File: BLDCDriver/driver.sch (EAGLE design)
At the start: 7 parts, among them U1 QFN50P400X400X100-25NDRV8300D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

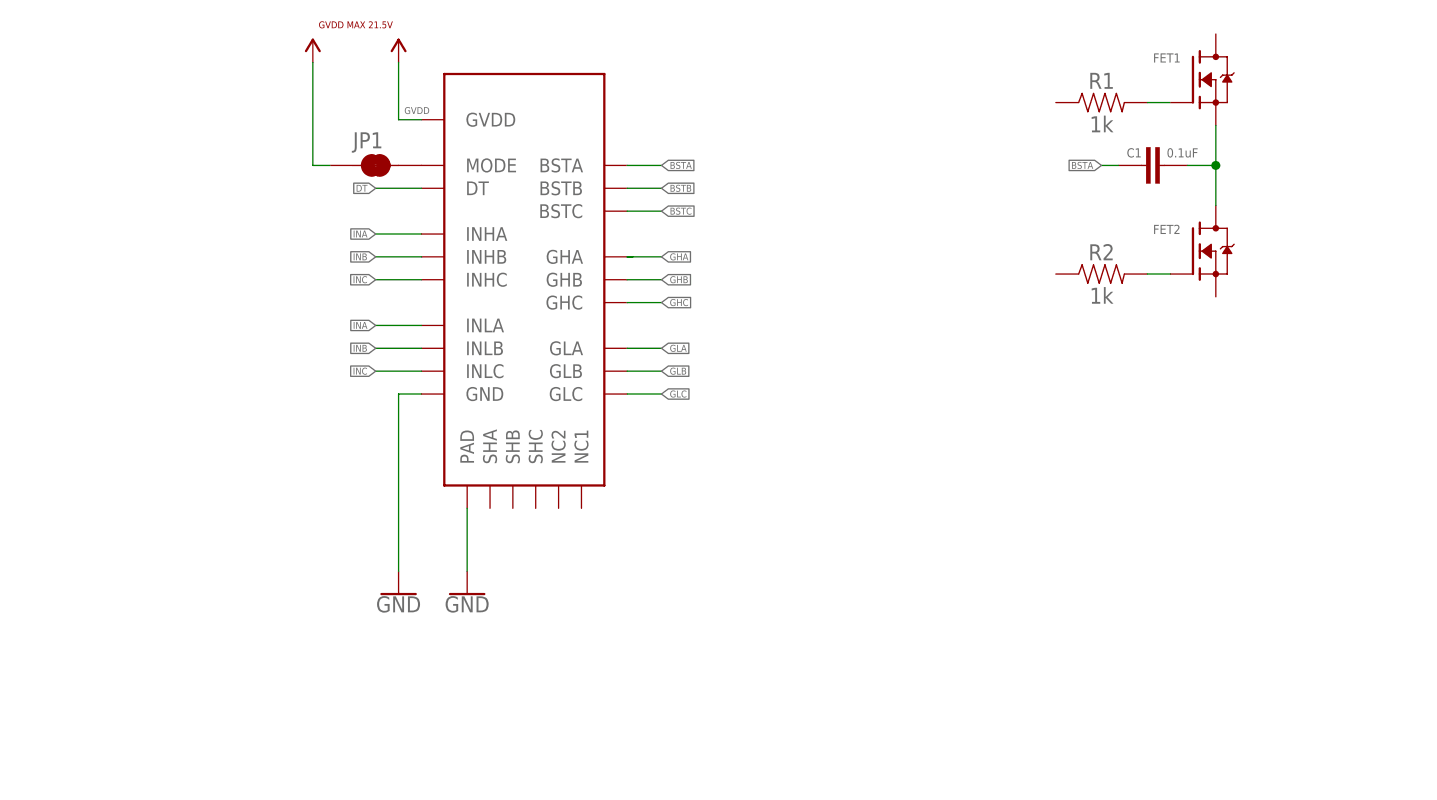
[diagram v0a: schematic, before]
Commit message: add MOSFETs on driver schematic
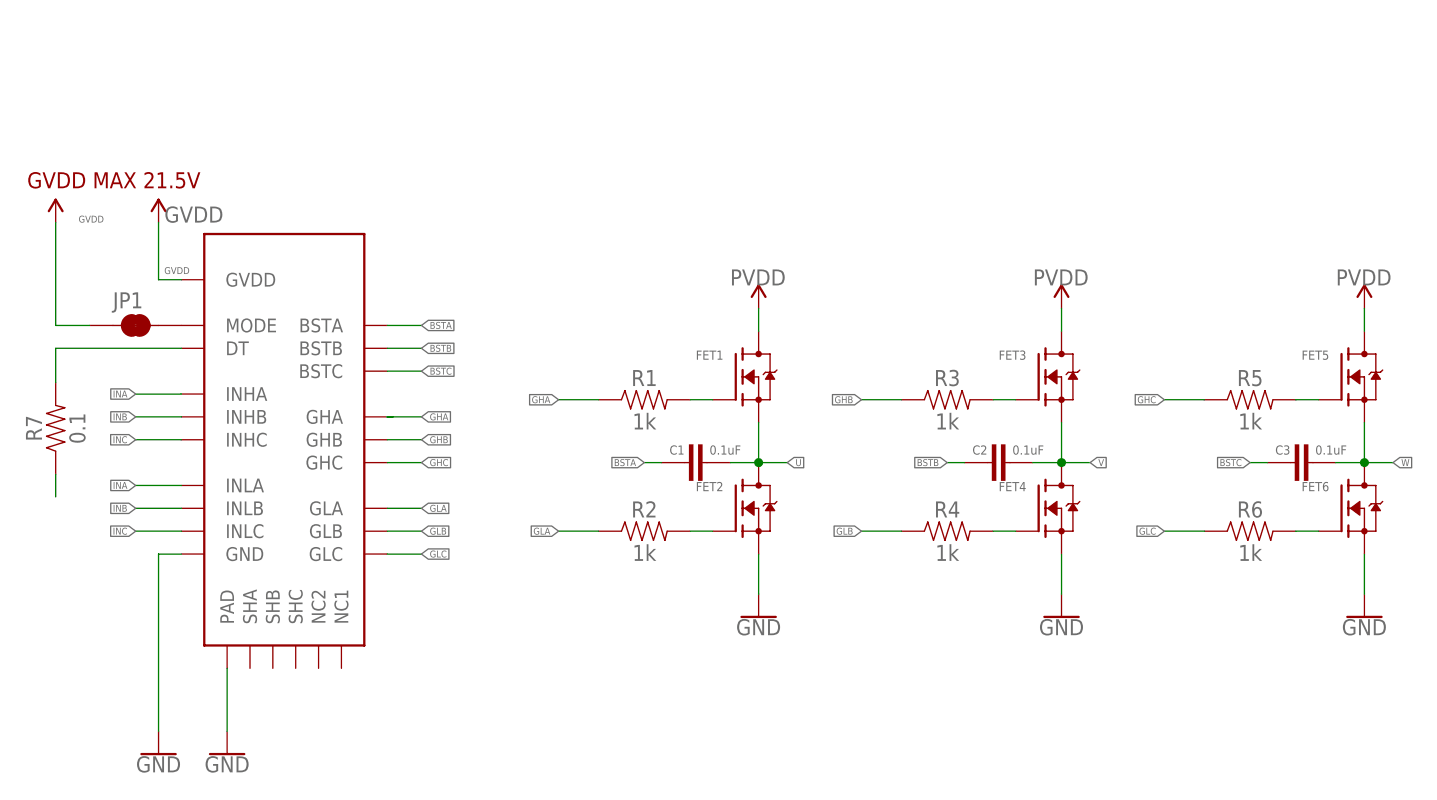
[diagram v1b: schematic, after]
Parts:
- added C2, C3: 0.1uF, SparkFun-Capacitors:0.1UF-0603-25V-5%
- added FET3, FET4, FET5, FET6: TPH11006NL, TPH11006NL:TPH11006NL
- added R3, R4, R5, R6: 1k, SparkFun-Resistors:1KOHM-0603-1/10W-1%
- added R7: 0.1, SparkFun-Resistors:1KOHM-0603-1/10W-1%
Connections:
- net N$1 renamed U
- new net N$1: FET3.G, R3.2
- new net N$5: FET4.G, R4.2
- new net N$6: FET5.G, R5.2
- new net N$7: FET6.G, R6.2
- new net N$8: R7.1
- new net PVDD: FET1.D, FET3.D, FET5.D
- new net V: C2.2, FET3.S, FET4.D
- new net W: C3.2, FET5.S, FET6.D
- net BSTB: now also C2.1
- net BSTC: now also C3.1
- net DT: now also R7.2
- net GHA: now also R1.1
- net GHB: now also R3.1
- net GHC: now also R5.1
- net GLA: now also R2.1
- net GLB: now also R4.1
- net GLC: now also R6.1
- net GND: now also FET2.S, FET4.S, FET6.S
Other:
- moved on the sheet: C1, FET1, FET2, JP1, R1, R2

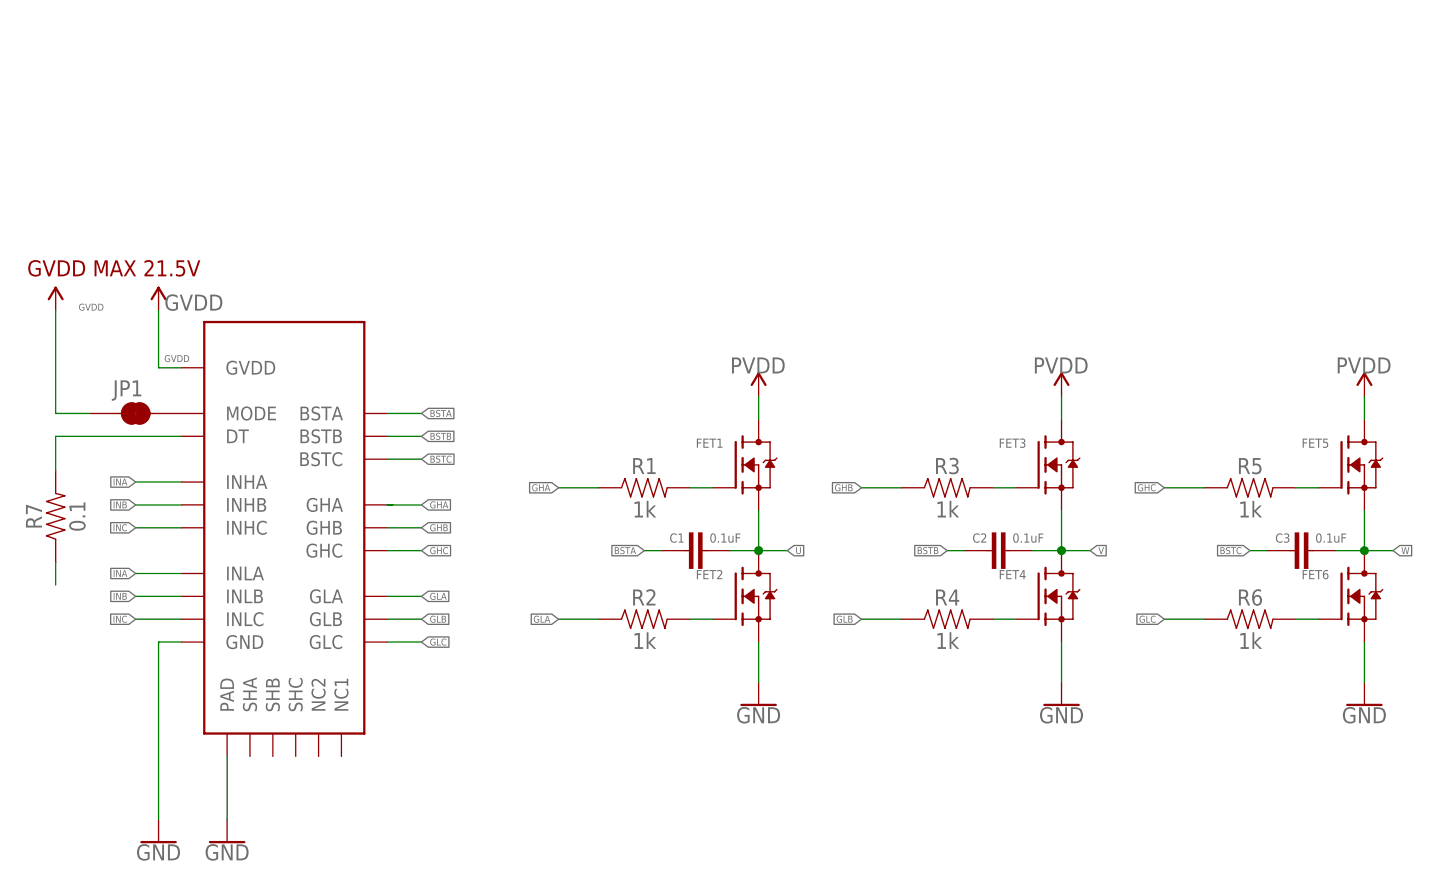
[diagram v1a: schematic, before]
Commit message: ゲートドライバを50Ωに決定した
詳しくは https://www.notion.so/rionessl/MOSFET-c3f0bc53d559421c83d572cacaf1d697#0553bd1ca6b7412ab2f7f6d7e1a45fa8
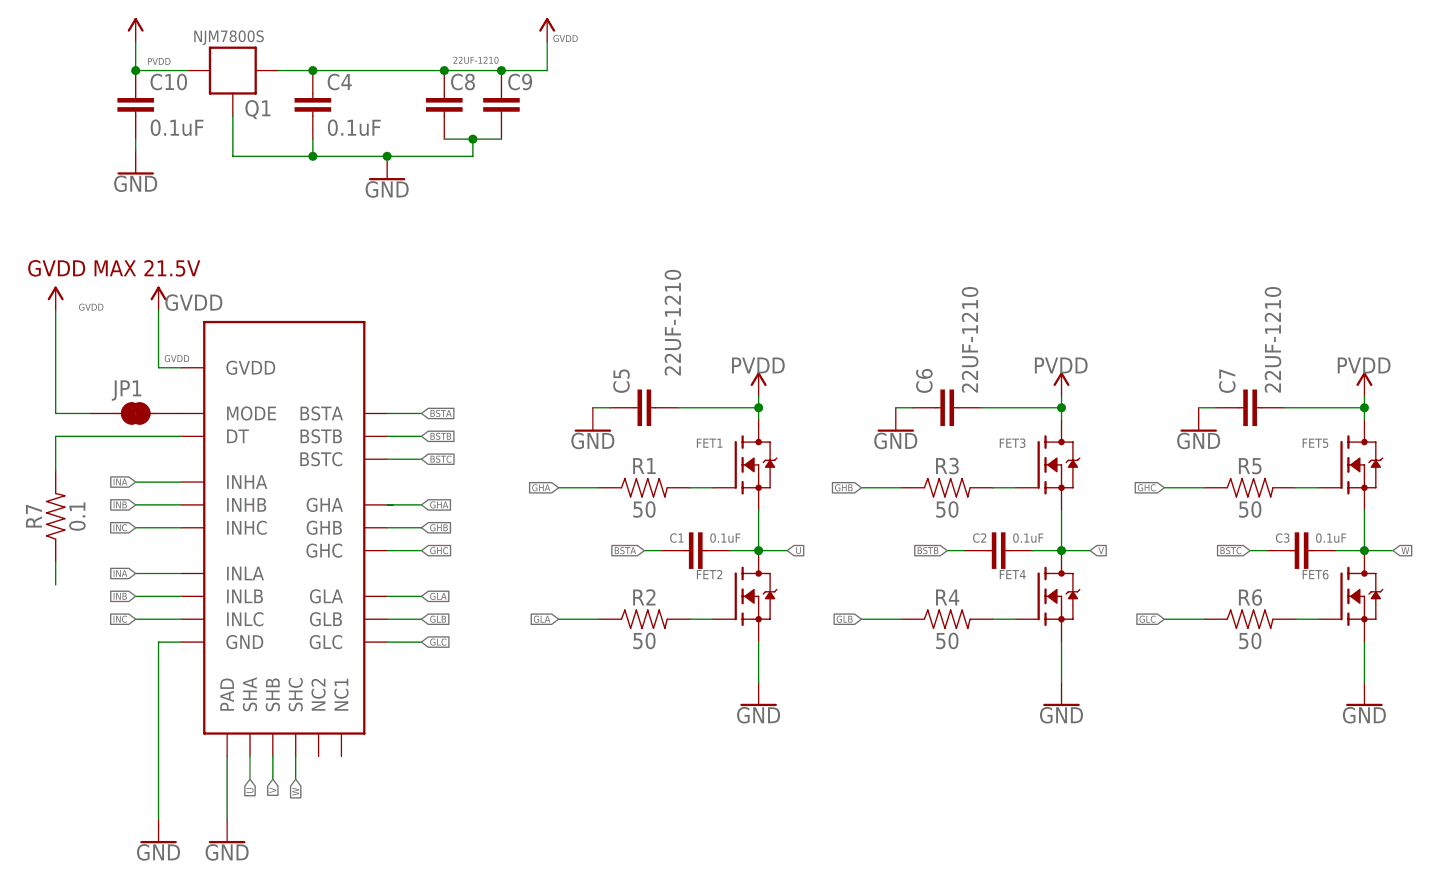
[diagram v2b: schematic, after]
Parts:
- added C10, C4: 0.1uF, SparkFun-Capacitors:0.1UF-0603-100V-10%
- added C5, C6, C7, C8, C9: 22UF-1210, SparkFun-Capacitors:22UF-1210-16V-20%
- added Q1: NJM7800S, NJM7800S:NJM7800S
- R1, R2, R3, R4, R5, R6: value 1k -> 50
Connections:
- net GND: now also C10.2, C4.2, C5.1, C6.1, C7.1, C8.1, C9.1, Q1.G
- net GVDD: now also C4.1, C8.2, C9.2, Q1.O
- net PVDD: now also C10.1, C5.2, C6.2, C7.2, Q1.I
- net U: now also U1.SHA
- net V: now also U1.SHB
- net W: now also U1.SHC

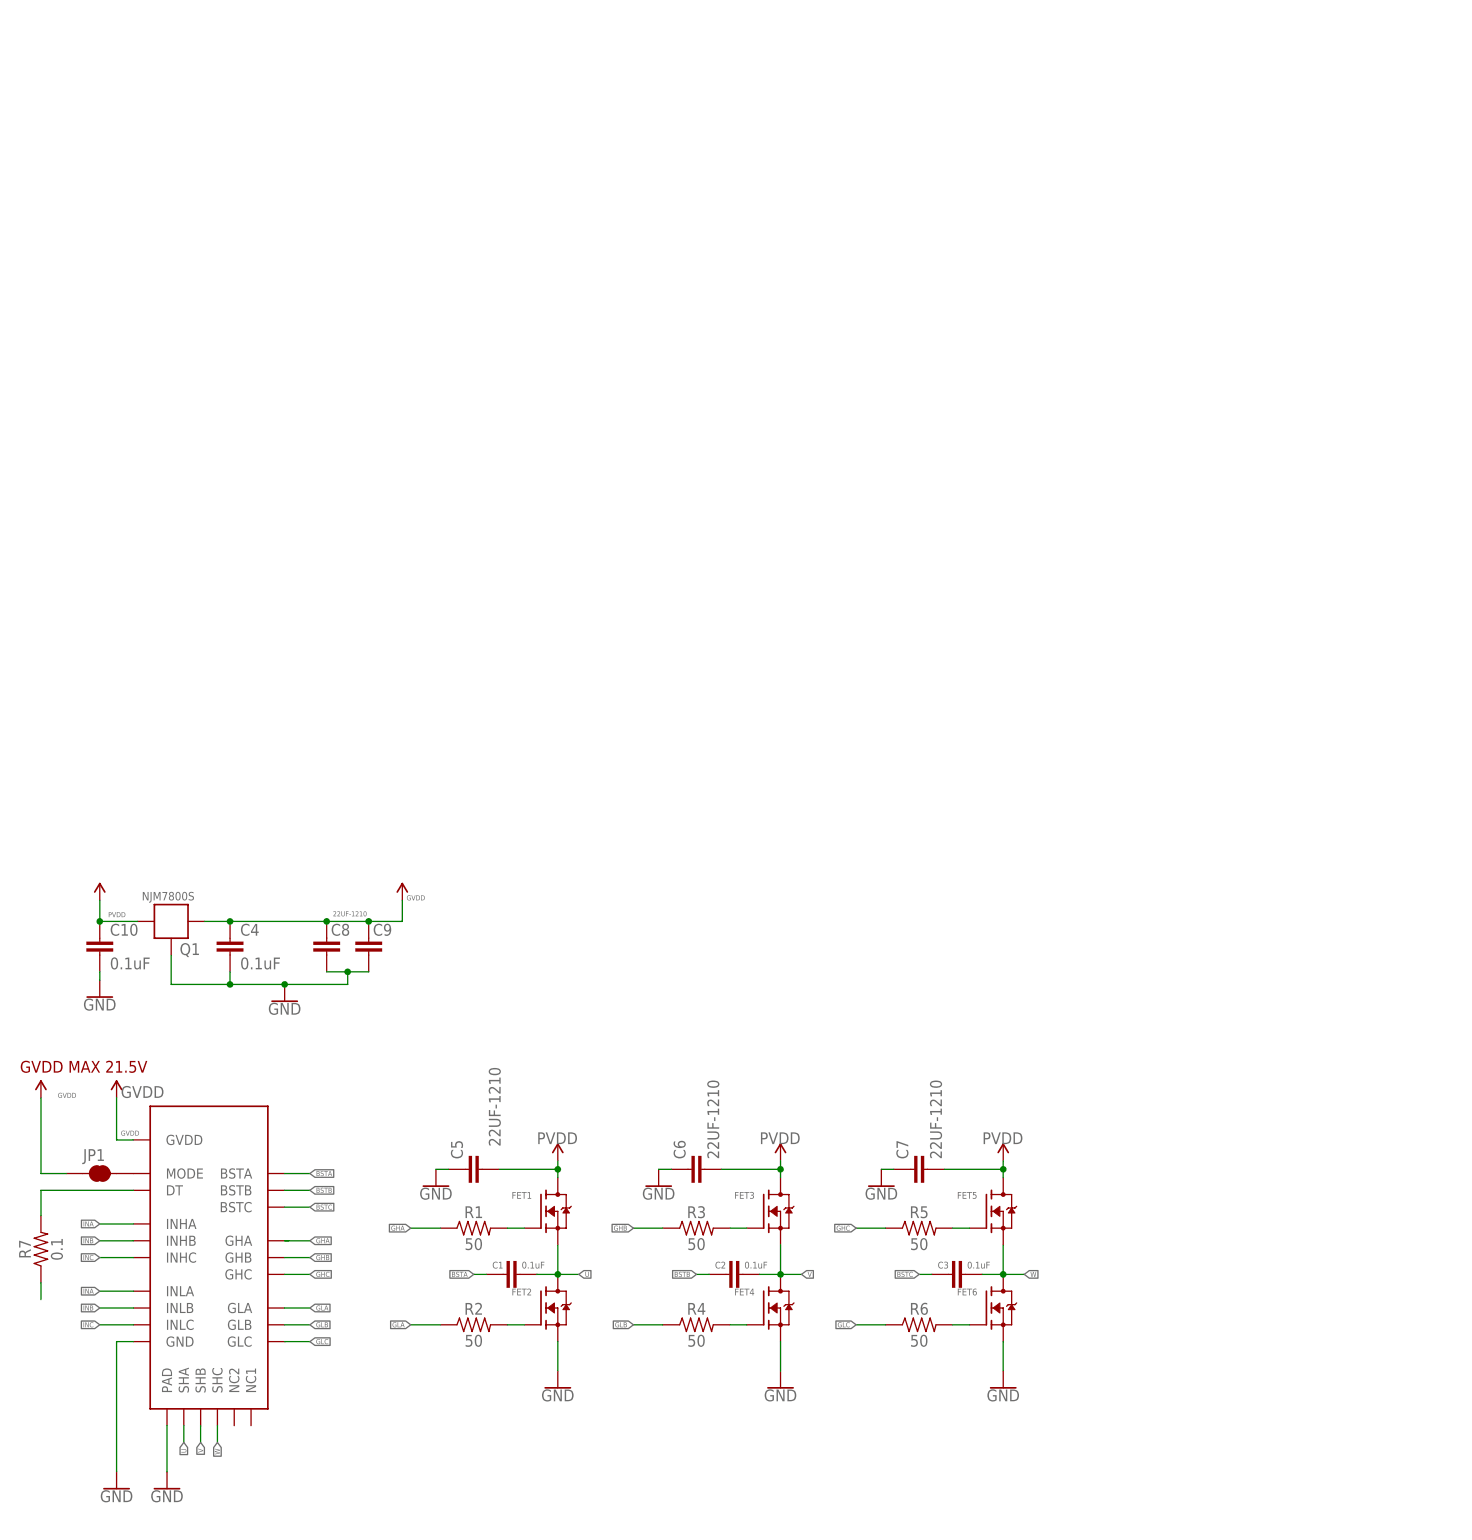
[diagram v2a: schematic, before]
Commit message: CurrentSenseを追加した
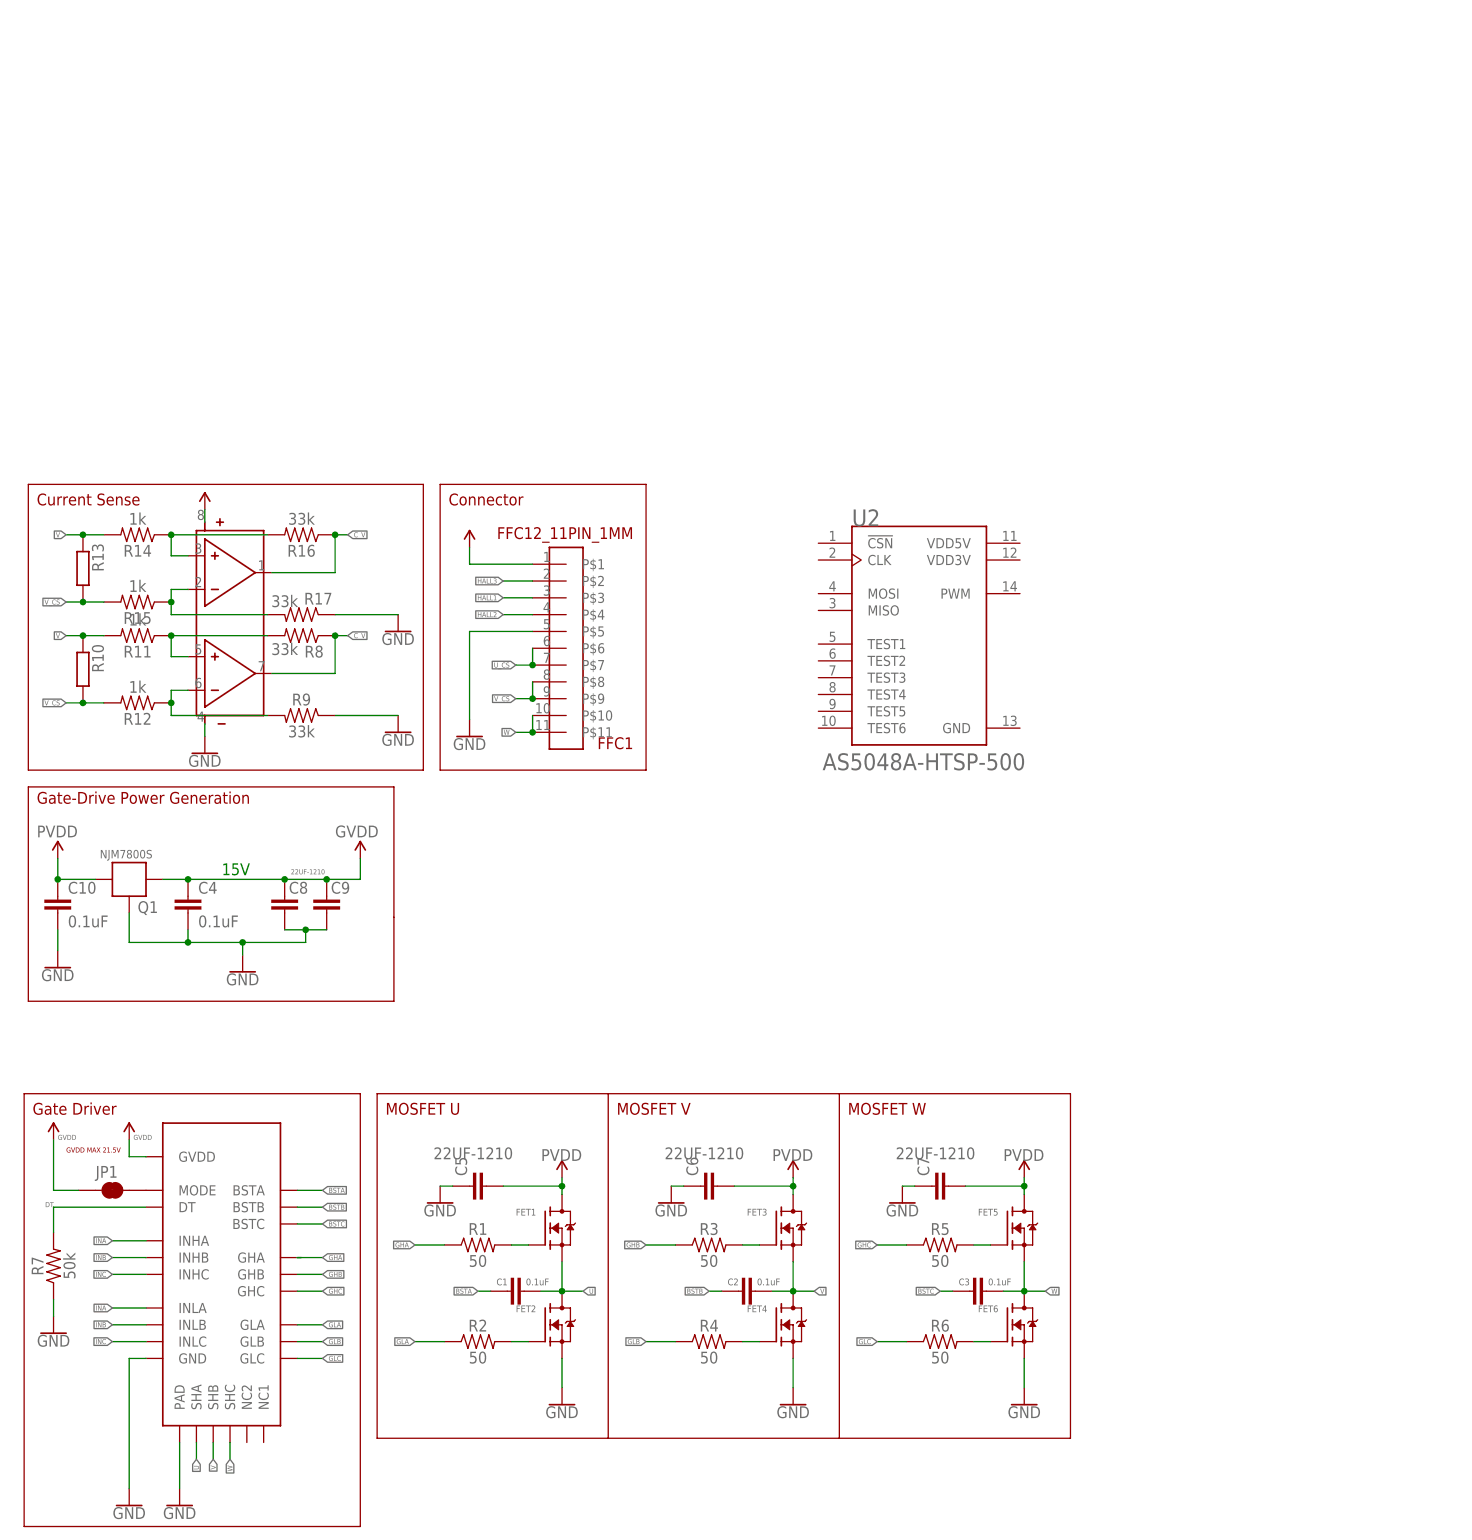
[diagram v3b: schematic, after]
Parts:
- added FFC1: FFC12_11PIN_1MM, MotorDriver_FourthEdition_prot:FFC12_11PIN_1MM
- added R10, R13: (no value), resistor-shunt:SMS-REF
- added R11, R12, R14, R15: 1k, SparkFun-Resistors:1KOHM-0603-1/10W-1%
- added R16, R17, R8, R9: 33k, SparkFun-Resistors:1KOHM-0603-1/10W-1%
- added U2: AS5048A-HTSP-500, AS5048A-HTSP-500:AS5048A-HTSP-500
- added U4: SOP80P620X125-8N, NJM2732:SOP80P620X125-8N
- R7: value 0.1 -> 50k
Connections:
- new net 3V3: U4.VDD
- new net 5V: FFC1.P$1
- new net C_V: R16.1, R8.1, U4.O1, U4.O2
- new net HALL1: FFC1.P$3
- new net HALL2: FFC1.P$4
- new net HALL3: FFC1.P$2
- new net N$10: R14.1, R16.2, U4.P1
- new net N$11: R15.1, R17.2, U4.M1
- new net N$9: R12.1, R9.2, U4.M2
- new net U_CS: FFC1.P$6, FFC1.P$7
- new net V_CS: FFC1.P$8, FFC1.P$9, R10.1, R12.2, R13.1, R15.2
- net GND: now also FFC1.P$5, R17.1, R7.1, R9.1, U4.GND
- net N$8: now also R11.1, R8.2, U4.P2; no longer R7.1
- net V: now also R10.2, R11.2, R13.2, R14.2
- net W: now also FFC1.P$10, FFC1.P$11
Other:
- note added: "15V"
- note added: "Connector"
- note added: "Current Sense"
- note added: "Gate Driver"
- note added: "Gate-Drive Power Generation"
- note added: "MOSFET U"
- note added: "MOSFET V"
- note added: "MOSFET W"
- moved on the sheet: C1, C10, C2, C3, C4, C5, C6, C7, C8, C9, FET1, FET2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
